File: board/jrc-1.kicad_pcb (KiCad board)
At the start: 4 copper layers, 200 x 100 mm, 81 parts, among them J1 USER PORT, J2 SERIAL A, J3 SERIAL B, J4 SD CARD, J5 DC IN 5V, J6 SLOT 1, J7 JTAG, J8 SLOT 2, J9 SLOT 3, SW1 SW_Push, SW2 SW_Push, U1 74HC21, U10 MAX238, U11 MAX238, U12 AS6C4008, U13 AS6C4008, U14 W29C020C, U15 74AC74, U16 8.0M, U17 DS1813, U18 DS1813, U19 JIGL, U2 W65C816SxPL, U20 SPI-65B, U3 74ACT245, U4 74AC573, U5 74ACT245, U6 74ACT245, U7 W65C22SxPL, U8 3.6864M, U9 SC28L92

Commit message: Use custom footprint for slots to get more favorable pin numbering for layout purposes.
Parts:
- added C46: 0.1u, Capacitor_THT:C_Rect_L4.6mm_W2.0mm_P2.50mm_MKS02_FKP02, F.Cu at (-253.2, 259.2)
- added U21: SN74AHCT245N, Package_DIP:DIP-20_W7.62mm_Socket, F.Cu at (154.0, 59.1)
- C13, C14, C15, C16, C17, C18, C19, C22: value 1.0u -> 0.1u; footprint Capacitor_THT:CP_Radial_D5.0mm_P2.00mm -> Capacitor_THT:C_Rect_L4.6mm_W2.0mm_P2.50mm_MKS02_FKP02
- C20: value 1.0u -> 10u
- C21: value 1.0u -> 100u
- C24, C26: value 0.1u -> 10u; footprint Capacitor_THT:C_Rect_L4.6mm_W2.0mm_P2.50mm_MKS02_FKP02 -> Capacitor_THT:CP_Radial_D5.0mm_P2.00mm
- C31, C35, C37: value 10u -> 1.0u
- C32: value 100u -> 1.0u
- C33, C34, C36, C38, C39, C40: value 0.1u -> 1.0u; footprint Capacitor_THT:C_Rect_L4.6mm_W2.0mm_P2.50mm_MKS02_FKP02 -> Capacitor_THT:CP_Radial_D5.0mm_P2.00mm
- C41, C42, C43, C44: value 0.1u -> 1u; footprint Capacitor_THT:C_Rect_L4.6mm_W2.0mm_P2.50mm_MKS02_FKP02 -> Capacitor_THT:CP_Radial_D5.0mm_P2.00mm
- J6, J8, J9: footprint Connector_Samtec_HLE_THT:Samtec_HLE-120-02-xx-DV-TE_2x20_P2.54mm_Horizontal -> jrc:JRC_Expansion_Slot
- U1: value 74HC21 -> AS6C4008; footprint Package_DIP:DIP-14_W7.62mm_Socket -> Package_DIP:DIP-32_W15.24mm
- U10, U11: value MAX238 -> DS1813; footprint Package_DIP:DIP-24_W7.62mm_Socket -> jrc:TO-92_reverse
- U12: value AS6C4008 -> 3.6864M; footprint Package_DIP:DIP-32_W15.24mm -> Package_DIP:DIP-8_W7.62mm_Socket
- U13: value AS6C4008 -> SC28L92; footprint Package_DIP:DIP-32_W15.24mm -> Package_LCC:PLCC-44_THT-Socket
- U14: value W29C020C -> MAX238; footprint Socket:DIP_Socket-32_W11.9_W12.7_W15.24_W17.78_W18.5_3M_232-1285-00-0602J -> Package_DIP:DIP-24_W7.62mm_Socket
- U15: value 74AC74 -> MAX238; footprint Package_DIP:DIP-14_W7.62mm_Socket -> Package_DIP:DIP-24_W7.62mm_Socket
- U16: value 8.0M -> W65C22SxPL; footprint Package_DIP:DIP-8_W7.62mm_Socket -> Package_LCC:PLCC-44_THT-Socket
- U17: value DS1813 -> CD74AC541E; footprint jrc:TO-92_reverse -> Package_DIP:DIP-20_W7.62mm_Socket
- U18: value DS1813 -> SN74AC74N; footprint jrc:TO-92_reverse -> Package_DIP:DIP-14_W7.62mm_Socket
- U19: value JIGL -> CD74AC541E; footprint Package_LCC:PLCC-44_THT-Socket -> Package_DIP:DIP-20_W7.62mm_Socket
- U2: value W65C816SxPL -> AS6C4008; footprint Package_LCC:PLCC-44_THT-Socket -> Package_DIP:DIP-32_W15.24mm
- U20: value SPI-65B -> 8.0M; footprint Package_LCC:PLCC-44_THT-Socket -> Package_DIP:DIP-8_W7.62mm_Socket
- U3: value 74ACT245 -> W29C020C; footprint Package_DIP:DIP-20_W7.62mm_Socket -> Socket:DIP_Socket-32_W11.9_W12.7_W15.24_W17.78_W18.5_3M_232-1285-00-0602J
- U4: value 74AC573 -> JIGL; footprint Package_DIP:DIP-20_W7.62mm_Socket -> Package_LCC:PLCC-44_THT-Socket
- U5: value 74ACT245 -> SPI-65B; footprint Package_DIP:DIP-20_W7.62mm_Socket -> Package_LCC:PLCC-44_THT-Socket
- U6: value 74ACT245 -> SN74HC21N; footprint Package_DIP:DIP-20_W7.62mm_Socket -> Package_DIP:DIP-14_W7.62mm_Socket
- U7: value W65C22SxPL -> W65C816SxPL
- U8: value 3.6864M -> SN74AHCT245N; footprint Package_DIP:DIP-8_W7.62mm_Socket -> Package_DIP:DIP-20_W7.62mm_Socket
- U9: value SC28L92 -> SN74AC573N; footprint Package_LCC:PLCC-44_THT-Socket -> Package_DIP:DIP-20_W7.62mm_Socket
- moved R1 612.7 mm to (-339.4, 21.7)
- moved R2 612.7 mm to (-339.4, 25.7)
- moved C41 578.6 mm to (-338.6, 31.0)
- moved U16 576.2 mm to (-266.5, 244.4)
- moved C43 546.7 mm to (-278.2, 266.8)
- moved C44 521.6 mm to (-288.4, 268.3)
- moved U2 515.3 mm to (-269.4, 165.9)
- moved C23 471.0 mm to (-141.8, 231.9)
- moved U1 470.6 mm to (-287.8, 165.9)
- moved C24 469.6 mm to (-141.7, 226.8)
- moved C27 464.1 mm to (-149.3, 197.7)
- moved C25 462.9 mm to (-129.1, 221.2)
- moved RN1 462.0 mm to (-233.1, 267.2)
- moved U20 454.8 mm to (-164.2, 298.4)
- moved C42 454.6 mm to (-170.6, 307.6)
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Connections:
- C13 pad 1: Net-(C13-Pad1) -> +5V
- C13 pad 2: Net-(C13-Pad2) -> GND
- C14 pad 1: Net-(C14-Pad1) -> +5V
- C14 pad 2: Net-(C14-Pad2) -> GND
- C15 pad 1: Net-(C15-Pad1) -> +5V
- C15 pad 2: Net-(C15-Pad2) -> GND
- C16 pad 1: Net-(C16-Pad1) -> +5V
- C16 pad 2: Net-(C16-Pad2) -> GND
- C19 pad 2: Net-(C19-Pad2) -> GND
- C20 pad 1: GND -> +5V
- C20 pad 2: Net-(C20-Pad2) -> GND
- C21 pad 2: Net-(C21-Pad2) -> GND
- C22 pad 1: GND -> +5V
- C22 pad 2: Net-(C22-Pad2) -> GND
- C31 pad 1: +5V -> Net-(C31-Pad1)
- C31 pad 2: GND -> Net-(C31-Pad2)
- C32 pad 1: +5V -> Net-(C32-Pad1)
- C32 pad 2: GND -> Net-(C32-Pad2)
- C33 pad 1: +5V -> Net-(C33-Pad1)
- C33 pad 2: GND -> Net-(C33-Pad2)
- C34 pad 1: +5V -> Net-(C34-Pad1)
- C34 pad 2: GND -> Net-(C34-Pad2)
- C37 pad 2: GND -> Net-(C37-Pad2)
- C38 pad 1: +5V -> GND
- C38 pad 2: GND -> Net-(C38-Pad2)
- C39 pad 2: GND -> Net-(C39-Pad2)
- C40 pad 1: +5V -> GND
- C40 pad 2: GND -> Net-(C40-Pad2)
- J6 pad 12: PHI2 -> XPHI2
- J6 pad 13: RWB -> XRWB
- J6 pad 14: RDB -> XRDB
- J6 pad 15: WRB -> XWRB
- J8 pad 12: PHI2 -> XPHI2
- J8 pad 13: RWB -> XRWB
- J8 pad 14: RDB -> XRDB
- J8 pad 15: WRB -> XWRB
- J9 pad 12: PHI2 -> XPHI2
- J9 pad 13: RWB -> XRWB
- J9 pad 14: RDB -> XRDB
- J9 pad 15: WRB -> XWRB
- U1 pad 1: VIAIRQB -> A18
- U1 pad 10: GND -> A2
- U1 pad 11: (no net) -> A1
- U1 pad 12: GND -> A0
- U1 pad 13: GND -> D0
- U1 pad 14: +5V -> D1
- U1 pad 2: UARTIRQB -> A16
- U1 pad 3: (no net) -> A14
- U1 pad 4: SPIIRQB -> A12
- U1 pad 5: SLOTIRQB -> A7
- U1 pad 6: Net-(U1-Pad6) -> A6
- U1 pad 7: GND -> A5
- U1 pad 8: (no net) -> A4
- U1 pad 9: GND -> A3
- U10 pad 1: RTSA -> RESETB
- U10 pad 2: TXDA -> +5V
- U10 pad 3: CTSA -> GND
- U11 pad 1: RTSB -> NMIB
- U11 pad 2: TXDB -> +5V
- U11 pad 3: CTSB -> GND
- U12 pad 1: A18 -> (no net)
- U12 pad 2: A16 -> (no net)
- U12 pad 3: A14 -> (no net)
- U12 pad 4: A12 -> GND
- U12 pad 5: A7 -> Net-(U12-Pad5)
- U12 pad 6: A6 -> (no net)
- U12 pad 7: A5 -> (no net)
- U12 pad 8: A4 -> +5V
- U13 pad 1: A18 -> (no net)
- U13 pad 10: A2 -> RDB
- U13 pad 11: A1 -> Net-(U13-Pad11)
- U13 pad 12: A0 -> (no net)
- U13 pad 13: D0 -> Net-(U13-Pad13)
- U13 pad 14: D1 -> Net-(U13-Pad14)
- U13 pad 15: D2 -> Net-(U13-Pad15)
- U13 pad 16: GND -> (no net)
- U13 pad 17: D3 -> (no net)
- U13 pad 18: D4 -> D1
- U13 pad 19: D5 -> D3
- U13 pad 2: A16 -> A0
- U13 pad 20: D6 -> D5
- U13 pad 22: RAM2CSB -> GND
- U13 pad 23: A10 -> (no net)
- U13 pad 24: RDB -> UARTIRQB
- U13 pad 25: A11 -> D6
- U13 pad 26: A9 -> D4
- U13 pad 27: A8 -> D2
- U13 pad 28: A13 -> D0
- U13 pad 29: WRB -> (no net)
- U13 pad 3: A14 -> Net-(U13-Pad3)
- U13 pad 30: A17 -> (no net)
- U13 pad 31: A15 -> Net-(U13-Pad31)
- U13 pad 32: +5V -> Net-(U13-Pad32)
- U13 pad 4: A12 -> A1
- U13 pad 5: A7 -> Net-(U13-Pad5)
- U13 pad 6: A6 -> A2
- U13 pad 7: A5 -> A3
- U13 pad 8: A4 -> Net-(U13-Pad8)
- U13 pad 9: A3 -> WRB
- U14 pad 1: (no net) -> RTSA
- U14 pad 10: A2 -> Net-(C31-Pad1)
- U14 pad 11: A1 -> Net-(C37-Pad2)
- U14 pad 12: A0 -> Net-(C31-Pad2)
- U14 pad 13: D0 -> Net-(C32-Pad1)
- U14 pad 14: D1 -> Net-(C32-Pad2)
- U14 pad 15: D2 -> Net-(C38-Pad2)
- U14 pad 16: GND -> DSRA
- U14 pad 17: D3 -> Net-(U13-Pad42)
- U14 pad 18: D4 -> Net-(U13-Pad32)
- U14 pad 19: D5 -> Net-(U13-Pad31)
- U14 pad 2: A16 -> TXDA
- U14 pad 20: D6 -> (no net)
- U14 pad 21: D7 -> (no net)
- U14 pad 22: ROMCSB -> Net-(U13-Pad40)
- U14 pad 23: A10 -> DCDA
- U14 pad 24: RDB -> DTRA
- U14 pad 3: A15 -> CTSA
- U14 pad 4: A12 -> Net-(U13-Pad8)
- U14 pad 5: A7 -> Net-(U13-Pad33)
- U14 pad 6: A6 -> Net-(U13-Pad35)
- U14 pad 7: A5 -> RxDA
- U14 pad 8: A4 -> GND
- U14 pad 9: A3 -> +5V
- U15 pad 1: +5V -> RTSB
- U15 pad 10: +5V -> Net-(C33-Pad1)
- U15 pad 11: +5V -> Net-(C39-Pad2)
- U15 pad 12: +5V -> Net-(C33-Pad2)
- U15 pad 13: +5V -> Net-(C34-Pad1)
- U15 pad 14: +5V -> Net-(C34-Pad2)
- U15 pad 2: Net-(R2-Pad2) -> TXDB
- U15 pad 3: Net-(U15-Pad3) -> CTSB
- U15 pad 4: +5V -> Net-(U13-Pad5)
- U15 pad 5: Net-(R1-Pad2) -> Net-(U13-Pad13)
- U15 pad 6: Net-(R2-Pad2) -> Net-(U13-Pad11)
- U15 pad 7: GND -> RxDB
- U15 pad 8: (no net) -> GND
- U15 pad 9: (no net) -> +5V
- U16 pad 1: (no net) -> GND
- U16 pad 2: (no net) -> PA0
- U16 pad 3: (no net) -> PA1
- U16 pad 4: GND -> PA2
- U16 pad 5: Net-(U15-Pad3) -> PA3
- U16 pad 6: (no net) -> PA4
- U16 pad 7: (no net) -> PA5
- U16 pad 8: +5V -> PA6
- U17 pad 1: RESETB -> GND
- U17 pad 2: +5V -> PHI2
- U17 pad 3: GND -> RWB
- U18 pad 1: NMIB -> +5V
- U18 pad 2: +5V -> Net-(R2-Pad2)
- U18 pad 3: GND -> Net-(U18-Pad3)
- U19 pad 1: A9 -> GND
- U19 pad 11: SLOTENB -> XA7
- U19 pad 12: SLOT1SELB -> XA6
- U19 pad 13: TMS -> XA5
- U19 pad 14: A16 -> XA4
- U19 pad 15: +5V -> XA3
- U19 pad 16: VPA -> XA2
- U19 pad 17: RESETB -> XA1
- U19 pad 18: RAM1CSB -> XA0
- U19 pad 19: ROMCSB -> GND
- U19 pad 2: A15 -> A0
- U19 pad 20: RAM2CSB -> +5V
- U19 pad 3: +5V -> A1
- U19 pad 4: Net-(U19-Pad4) -> A2
- U19 pad 5: SLOT3SELB -> A3
- U19 pad 6: SLOT2SELB -> A4
- U19 pad 7: TDI -> A5
- U19 pad 8: VIASELB -> A6
- U19 pad 9: UARTSELB -> A7
- U2 pad 1: GND -> A18
- U2 pad 10: A0 -> A2
- U2 pad 12: (no net) -> A0
- U2 pad 13: A2 -> D0
- U2 pad 14: A3 -> D1
- U2 pad 15: A4 -> D2
- U2 pad 16: A5 -> GND
- U2 pad 17: A6 -> D3
- U2 pad 18: A7 -> D4
- U2 pad 19: A8 -> D5
- U2 pad 2: (no net) -> A16
- U2 pad 20: A9 -> D6
- U2 pad 21: A10 -> D7
- U2 pad 22: A11 -> RAM2CSB
- U2 pad 23: GND -> A10
- U2 pad 24: GND -> RDB
- U2 pad 25: A12 -> A11
- U2 pad 26: A13 -> A9
- U2 pad 27: A14 -> A8
- U2 pad 28: A15 -> A13
- U2 pad 29: Net-(U2-Pad29) -> WRB
- U2 pad 3: Net-(RN1-Pad4) -> A14
- U2 pad 30: Net-(U2-Pad30) -> A17
- U2 pad 31: Net-(U2-Pad31) -> A15
- U2 pad 32: Net-(U2-Pad32) -> +5V
- U2 pad 4: Net-(RN1-Pad5) -> A12
- U2 pad 5: Net-(U1-Pad6) -> A7
- U2 pad 6: (no net) -> A6
- U2 pad 7: NMIB -> A5
- U2 pad 8: VPA -> A4
- U2 pad 9: +5V -> A3
- U20 pad 2: MISO -> (no net)
- U20 pad 3: +5V -> (no net)
- U20 pad 4: D7 -> GND
- U20 pad 5: D5 -> Net-(U18-Pad3)
- U20 pad 6: D6 -> (no net)
- U20 pad 7: Net-(U19-Pad38) -> (no net)
- U20 pad 8: D4 -> +5V
- U3 pad 1: RWB -> (no net)
- U3 pad 10: GND -> A2
- U3 pad 11: Net-(U2-Pad29) -> A1
- U3 pad 12: Net-(U2-Pad30) -> A0
- U3 pad 13: Net-(U2-Pad31) -> D0
- U3 pad 14: Net-(U2-Pad32) -> D1
- U3 pad 15: Net-(U2-Pad33) -> D2
- U3 pad 16: Net-(U2-Pad34) -> GND
- U3 pad 17: Net-(U2-Pad35) -> D3
- U3 pad 18: Net-(U2-Pad36) -> D4
- U3 pad 19: PHI1 -> D5
- U3 pad 2: D0 -> A16
- U3 pad 20: +5V -> D6
- U3 pad 3: D1 -> A15
- U3 pad 4: D2 -> A12
- U3 pad 5: D3 -> A7
- U3 pad 6: D4 -> A6
- U3 pad 7: D5 -> A5
- U3 pad 8: D6 -> A4
- U3 pad 9: D7 -> A3
- U4 pad 1: GND -> A9
- U4 pad 11: PHI1 -> SLOTENB
- U4 pad 12: (no net) -> SLOT1SELB
- U4 pad 13: (no net) -> TMS
- U4 pad 14: (no net) -> A16
- U4 pad 15: A20 -> +5V
- U4 pad 16: A19 -> VPA
- U4 pad 17: A18 -> RESETB
- U4 pad 18: A17 -> RAM1CSB
- U4 pad 19: A16 -> ROMCSB
- U4 pad 2: Net-(U2-Pad36) -> A15
- U4 pad 20: +5V -> RAM2CSB
- U4 pad 3: Net-(U2-Pad35) -> +5V
- U4 pad 4: Net-(U2-Pad34) -> Net-(U4-Pad4)
- U4 pad 5: Net-(U2-Pad33) -> SLOT3SELB
- U4 pad 6: Net-(U2-Pad32) -> SLOT2SELB
- U4 pad 7: Net-(U2-Pad31) -> TDI
- U4 pad 8: Net-(U2-Pad30) -> VIASELB
- U4 pad 9: Net-(U2-Pad29) -> UARTSELB
- U5 pad 1: +5V -> (no net)
- U5 pad 11: XA7 -> D2
- U5 pad 12: XA6 -> SS0
- U5 pad 13: XA5 -> TMS
- U5 pad 14: XA4 -> D1
- U5 pad 15: XA3 -> +5V
- U5 pad 16: XA2 -> D0
- U5 pad 17: XA1 -> SS1
- U5 pad 18: XA0 -> SS3
- U5 pad 19: GND -> SS4
- U5 pad 2: A0 -> MISO
- U5 pad 20: +5V -> SS2
- U5 pad 3: A1 -> +5V
- U5 pad 4: A2 -> D7
- U5 pad 5: A3 -> D5
- U5 pad 6: A4 -> D6
- U5 pad 7: A5 -> Net-(U4-Pad38)
- U5 pad 8: A6 -> D4
- U5 pad 9: A7 -> D3
- U6 pad 1: RWB -> VIAIRQB
- U6 pad 11: D7 -> (no net)
- U6 pad 12: D6 -> GND
- U6 pad 13: D5 -> GND
- U6 pad 14: D4 -> +5V
- U6 pad 2: XD0 -> UARTIRQB
- U6 pad 3: XD1 -> (no net)
- U6 pad 4: XD2 -> SPIIRQB
- U6 pad 5: XD3 -> SLOTIRQB
- U6 pad 6: XD4 -> Net-(U6-Pad6)
- U6 pad 7: XD5 -> GND
- U6 pad 8: XD6 -> (no net)
- U6 pad 9: XD7 -> GND
- U7 pad 10: PB0 -> A0
- U7 pad 11: (no net) -> A1
- U7 pad 12: PB1 -> (no net)
- U7 pad 13: PB2 -> A2
- U7 pad 14: PB3 -> A3
- U7 pad 15: PB4 -> A4
- U7 pad 16: PB5 -> A5
- U7 pad 17: PB6 -> A6
- U7 pad 18: PB7 -> A7
- U7 pad 19: CB1 -> A8
- U7 pad 2: PA0 -> (no net)
- U7 pad 20: CB2 -> A9
- U7 pad 21: +5V -> A10
- U7 pad 22: (no net) -> A11
- U7 pad 23: VIAIRQB -> GND
- U7 pad 24: RWB -> GND
- U7 pad 25: VIASELB -> A12
- U7 pad 26: +5V -> A13
- U7 pad 27: PHI2 -> A14
- U7 pad 28: D7 -> A15
- U7 pad 29: D6 -> Net-(U7-Pad29)
- U7 pad 3: PA1 -> Net-(RN1-Pad4)
- U7 pad 30: D5 -> Net-(U7-Pad30)
- U7 pad 31: D4 -> Net-(U7-Pad31)
- U7 pad 32: D3 -> Net-(U7-Pad32)
- U7 pad 33: (no net) -> Net-(U7-Pad33)
- U7 pad 34: D2 -> Net-(U7-Pad34)
- U7 pad 35: D1 -> Net-(U7-Pad35)
- U7 pad 36: D0 -> Net-(U7-Pad36)
- U7 pad 37: RESETB -> +5V
- U7 pad 38: (no net) -> RWB
- U7 pad 39: A3 -> (no net)
- U7 pad 4: PA2 -> Net-(RN1-Pad5)
- U7 pad 40: A2 -> Net-(RN1-Pad3)
- U7 pad 41: A1 -> PHI2
- U7 pad 42: A0 -> (no net)
- U7 pad 43: CA2 -> VDA
- U7 pad 44: CA1 -> RESETB
- U7 pad 5: PA3 -> Net-(U6-Pad6)
- U7 pad 6: PA4 -> (no net)
- U7 pad 7: PA5 -> NMIB
- U7 pad 8: PA6 -> VPA
- U7 pad 9: PA7 -> +5V
- U8 pad 1: (no net) -> RWB
- U8 pad 2: (no net) -> D0
- U8 pad 3: (no net) -> D1
- U8 pad 4: GND -> D2
- U8 pad 5: Net-(U8-Pad5) -> D3
- U8 pad 6: (no net) -> D4
- U8 pad 7: (no net) -> D5
- U8 pad 8: +5V -> D6
- U9 pad 1: (no net) -> GND
- U9 pad 10: RDB -> GND
- U9 pad 11: Net-(U11-Pad6) -> PHI1
- U9 pad 13: Net-(U11-Pad5) -> (no net)
- U9 pad 14: Net-(U11-Pad18) -> (no net)
- U9 pad 15: Net-(U11-Pad19) -> A20
- U9 pad 16: (no net) -> A19
- U9 pad 17: (no net) -> A18
- U9 pad 18: D1 -> A17
- U9 pad 19: D3 -> A16
- U9 pad 2: A0 -> Net-(U7-Pad36)
- U9 pad 20: D5 -> +5V
- U9 pad 3: Net-(U11-Pad22) -> Net-(U7-Pad35)
- U9 pad 4: A1 -> Net-(U7-Pad34)
- U9 pad 5: Net-(U11-Pad4) -> Net-(U7-Pad33)
- U9 pad 6: A2 -> Net-(U7-Pad32)
- U9 pad 7: A3 -> Net-(U7-Pad31)
- U9 pad 8: Net-(U10-Pad4) -> Net-(U7-Pad30)
- U9 pad 9: WRB -> Net-(U7-Pad29)

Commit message: RC1 of schematic and initial board layout
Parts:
- removed the C19 at (-147.9, 232.1)
- removed the C20 at (-130.5, 216.2)
- removed the C24 at (-141.7, 226.8)
- removed the C26 at (-120.0, 207.7)
- removed the C29 at (-178.4, 197.8)
- removed the C31 at (-134.9, 167.1)
- removed the C33 at (-134.9, 173.7)
- removed C44: 1u, Capacitor_THT:CP_Radial_D5.0mm_P2.00mm
- removed C45, C46: 0.1u, Capacitor_THT:C_Rect_L4.6mm_W2.0mm_P2.50mm_MKS02_FKP02
- removed the U17 at (154.0, 89.2)
- removed U19: CD74AC541E, Package_DIP:DIP-20_W7.62mm_Socket
- removed U21: SN74AHCT245N, Package_DIP:DIP-20_W7.62mm_Socket
- added C27: 1.0u, Capacitor_THT:CP_Radial_D5.0mm_P2.00mm, F.Cu at (185.2, 97.4)
- added D1: POWER, LED_THT:LED_D5.0mm_Clear, F.Cu at (204.7, 143.0)
- added H1: MountingHole, MountingHole:MountingHole_2.7mm_M2.5, F.Cu at (27.4, 24.1)
- added H2: MountingHole, MountingHole:MountingHole_2.7mm_M2.5, F.Cu at (87.0, 10.7)
- added H3: MountingHole, MountingHole:MountingHole_2.7mm_M2.5, F.Cu at (215.0, 146.0)
- added H4: MountingHole, MountingHole:MountingHole_2.7mm_M2.5, F.Cu at (25.0, 146.0)
- added R3: 330, Resistor_THT:R_Axial_DIN0207_L6.3mm_D2.5mm_P10.16mm_Horizontal, F.Cu at (200.2, 143.0)
- C19: renamed from C21; footprint Capacitor_THT:CP_Radial_D5.0mm_P2.00mm -> Capacitor_THT:CP_Radial_D6.3mm_P2.50mm
- C25: value 0.1u -> 1.0u; footprint Capacitor_THT:C_Rect_L4.6mm_W2.0mm_P2.50mm_MKS02_FKP02 -> Capacitor_THT:CP_Radial_D5.0mm_P2.00mm
- C35: renamed from C41; value 1u -> 0.1u; footprint Capacitor_THT:CP_Radial_D5.0mm_P2.00mm -> Capacitor_THT:C_Rect_L4.6mm_W2.0mm_P2.50mm_MKS02_FKP02
- C36: renamed from C42; value 1u -> 0.1u; footprint Capacitor_THT:CP_Radial_D5.0mm_P2.00mm -> Capacitor_THT:C_Rect_L4.6mm_W2.0mm_P2.50mm_MKS02_FKP02
- C37: renamed from C43; value 1u -> 0.1u; footprint Capacitor_THT:CP_Radial_D5.0mm_P2.00mm -> Capacitor_THT:C_Rect_L4.6mm_W2.0mm_P2.50mm_MKS02_FKP02
- J1: footprint Connector_PinHeader_1.00mm:PinHeader_2x17_P1.00mm_Vertical -> Connector_PinHeader_2.54mm:PinHeader_2x17_P2.54mm_Vertical
- SW1: value SW_Push -> RESET
- SW2: value SW_Push -> NMI
- U1, U2: footprint Package_DIP:DIP-32_W15.24mm -> Package_DIP:DIP-32_W15.24mm_Socket
- moved R2 469.8 mm to (125.5, 93.8), turned to 270 degrees
- moved R1 466.9 mm to (121.9, 93.8), turned to 270 degrees
- moved C3 427.3 mm to (158.7, 46.7), turned to 270 degrees
- moved C37 422.4 mm to (105.9, 90.9), turned to 180 degrees
- moved U2 400.1 mm to (112.5, 46.6)
- moved U1 399.1 mm to (93.0, 46.6)
- moved C2 395.4 mm to (125.3, 43.4)
- moved C24 393.8 mm to (195.0, 93.0)
- moved U17 391.3 mm to (110.2, 94.2)
- moved C35 387.8 mm to (34.8, 135.6)
- moved C1 372.1 mm to (106.8, 43.4)
- moved C14 371.6 mm to (73.4, 40.9), turned to 180 degrees
- moved C22 363.7 mm to (183.9, 124.0), turned to 270 degrees
- moved C36 361.0 mm to (118.1, 90.9), turned to 180 degrees
- moved RN1 360.9 mm to (49.0, 42.2), turned to 180 degrees
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- renumbered C22 to C20, C27 to C21, C28 to C22, C30 to C24, C32 to C26, C34 to C28, C35 to C29, C36 to C30, C37 to C31, C38 to C32, C39 to C33, C40 to C34, U18 to U17, U20 to U18
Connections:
- C25 pad 1: +5V -> Net-(C25-Pad1)
- C25 pad 2: GND -> Net-(C25-Pad2)
- J6 pad 10: XA7 -> A0
- J6 pad 11: SLOT1SELB -> (no net)
- J6 pad 12: XPHI2 -> PHI2
- J6 pad 13: XRWB -> RWB
- J6 pad 14: XRDB -> RDB
- J6 pad 15: XWRB -> WRB
- J6 pad 18: (no net) -> SLOT1SELB
- J6 pad 23: XD0 -> D7
- J6 pad 24: XD1 -> D6
- J6 pad 25: XD2 -> D5
- J6 pad 26: XD3 -> D4
- J6 pad 27: XD4 -> D3
- J6 pad 28: XD5 -> D2
- J6 pad 29: XD6 -> D1
- J6 pad 3: XA0 -> A7
- J6 pad 30: XD7 -> D0
- J6 pad 32: SLOTIRQB -> (no net)
- J6 pad 38: (no net) -> SLOTIRQB
- J6 pad 4: XA1 -> A6
- J6 pad 5: XA2 -> A5
- J6 pad 6: XA3 -> A4
- J6 pad 7: XA4 -> A3
- J6 pad 8: XA5 -> A2
- J6 pad 9: XA6 -> A1
- J8 pad 10: XA7 -> A0
- J8 pad 11: SLOT2SELB -> (no net)
- J8 pad 12: XPHI2 -> PHI2
- J8 pad 13: XRWB -> RWB
- J8 pad 14: XRDB -> RDB
- J8 pad 15: XWRB -> WRB
- J8 pad 18: (no net) -> SLOT2SELB
- J8 pad 23: XD0 -> D7
- J8 pad 24: XD1 -> D6
- J8 pad 25: XD2 -> D5
- J8 pad 26: XD3 -> D4
- J8 pad 27: XD4 -> D3
- J8 pad 28: XD5 -> D2
- J8 pad 29: XD6 -> D1
- J8 pad 3: XA0 -> A7
- J8 pad 30: XD7 -> D0
- J8 pad 32: SLOTIRQB -> (no net)
- J8 pad 38: (no net) -> SLOTIRQB
- J8 pad 4: XA1 -> A6
- J8 pad 5: XA2 -> A5
- J8 pad 6: XA3 -> A4
- J8 pad 7: XA4 -> A3
- J8 pad 8: XA5 -> A2
- J8 pad 9: XA6 -> A1
- J9 pad 10: XA7 -> A0
- J9 pad 11: SLOT3SELB -> (no net)
- J9 pad 12: XPHI2 -> PHI2
- J9 pad 13: XRWB -> RWB
- J9 pad 14: XRDB -> RDB
- J9 pad 15: XWRB -> WRB
- J9 pad 18: (no net) -> SLOT3SELB
- J9 pad 23: XD0 -> D7
- J9 pad 24: XD1 -> D6
- J9 pad 25: XD2 -> D5
- J9 pad 26: XD3 -> D4
- J9 pad 27: XD4 -> D3
- J9 pad 28: XD5 -> D2
- J9 pad 29: XD6 -> D1
- J9 pad 3: XA0 -> A7
- J9 pad 30: XD7 -> D0
- J9 pad 32: SLOTIRQB -> (no net)
- J9 pad 38: (no net) -> SLOTIRQB
- J9 pad 4: XA1 -> A6
- J9 pad 5: XA2 -> A5
- J9 pad 6: XA3 -> A4
- J9 pad 7: XA4 -> A3
- J9 pad 8: XA5 -> A2
- J9 pad 9: XA6 -> A1
- U14 pad 10: Net-(C31-Pad1) -> Net-(C25-Pad1)
- U14 pad 12: Net-(C31-Pad2) (its old number) -> Net-(C25-Pad2)
- U4 pad 11: SLOTENB -> (no net)
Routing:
- net A1: track 0.00 -> 376.4 mm, vias 0 -> 1
- net A0: track 0.00 -> 366.6 mm, vias 0 -> 2
- net D2: track 0.00 -> 360.1 mm, vias 0 -> 2
- net D6: track 0.00 -> 359.7 mm
- net NMIB: track 0.00 -> 358.2 mm
- net D3: track 0.00 -> 353.3 mm, vias 0 -> 1
- net D0: track 0.00 -> 353.1 mm, vias 0 -> 2
- net RESETB: track 0.00 -> 347.7 mm
- net D5: track 0.00 -> 346.7 mm, vias 0 -> 1
- net D7: track 0.00 -> 344.9 mm
- net D4: track 0.00 -> 341.3 mm, vias 0 -> 2
- net A3: track 0.00 -> 338.9 mm
- net D1: track 0.00 -> 331.1 mm, vias 0 -> 2
- net A2: track 0.00 -> 327.9 mm, vias 0 -> 1
- net RWB: track 0.00 -> 305.6 mm, vias 0 -> 3
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- added copper zone on In2.Cu, net +5V
- added copper zone on In1.Cu, net GND
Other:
- board size 200 x 100 mm -> 200 x 130 mm
- net class Default: trace_width 0.25 -> 0.2; via_dia 0.8 -> 0.6; via_drill 0.4 -> 0.3
- rule trace_min: 0.2 -> 0.09
- rule via_min_drill: 0.3 -> 0.2
- board text added: "JRC-1 Single Board Computer Revision 1.0 (C) 2021 Joshua M. Thompson https://www.area73.us/jrc-1"

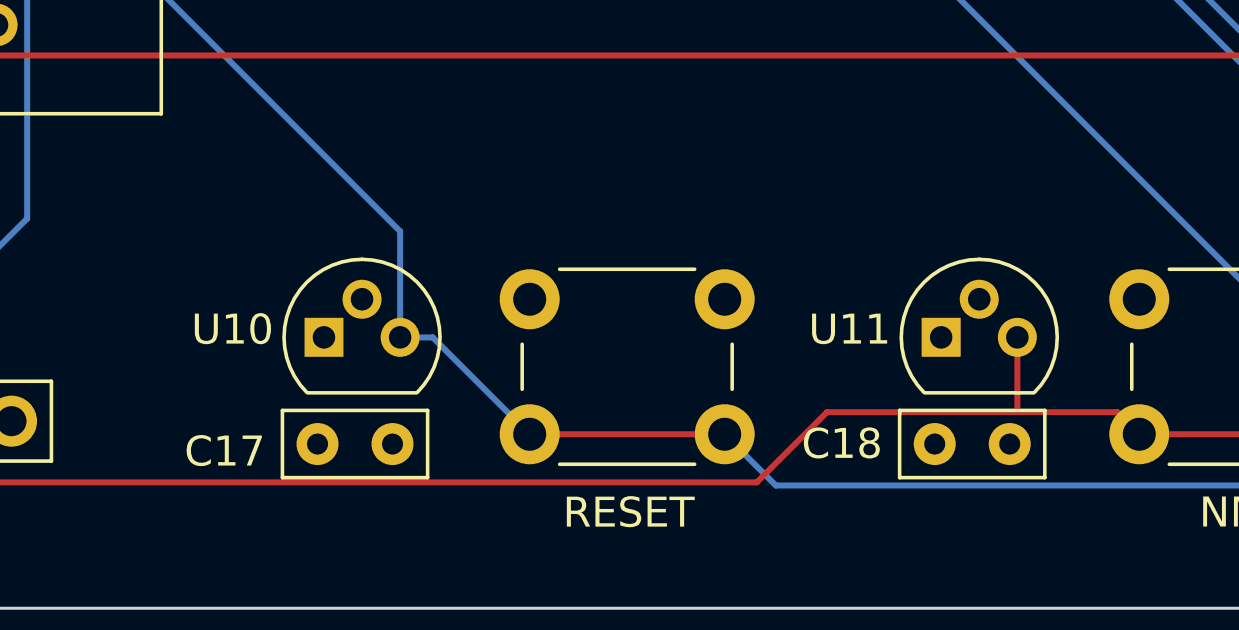
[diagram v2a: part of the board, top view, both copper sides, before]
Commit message: Fix footprint for RESET and NMI button handlers Fix symbol for '573 latch
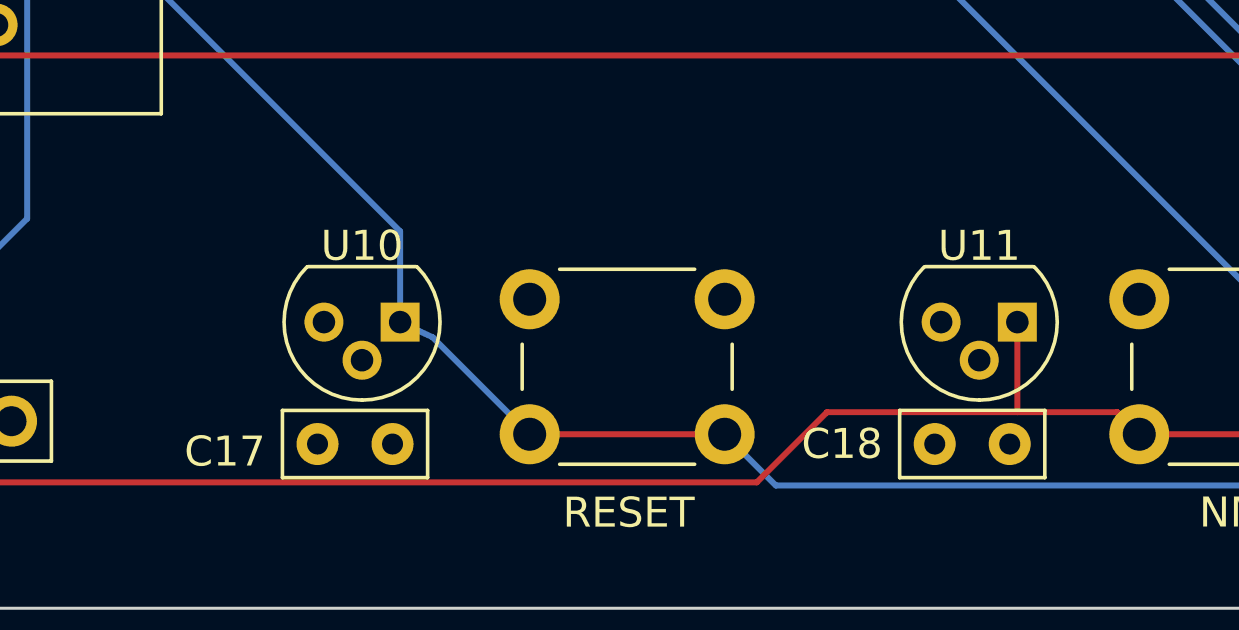
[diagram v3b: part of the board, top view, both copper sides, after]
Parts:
- U10, U11: footprint jrc:TO-92_reverse -> Package_TO_SOT_THT:TO-92
- moved U10 2.59 mm to (109.0, 140.5), turned to 180 degrees
- moved U11 2.59 mm to (129.5, 140.5), turned to 180 degrees
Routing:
- net NMIB: track 358.2 -> 358.7 mm
